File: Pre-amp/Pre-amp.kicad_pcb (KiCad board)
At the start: 2 copper layers, 80 x 53.3 mm, 52 parts, among them J1 In, J2 Send, J3 Return, J4 Out, J5 PWR, U1 LF353N, U2 LF353N, U3 LF353N

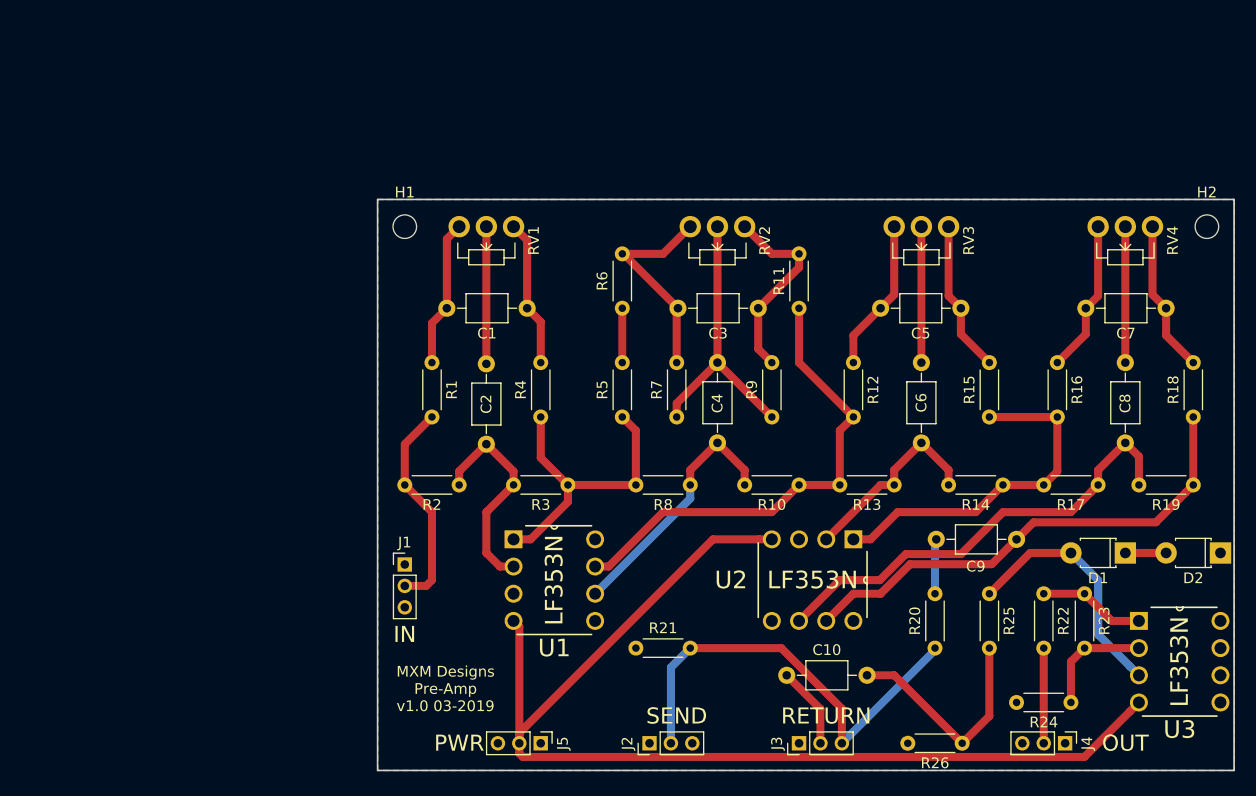
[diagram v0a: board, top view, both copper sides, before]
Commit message: Add buffer input to pre-amp
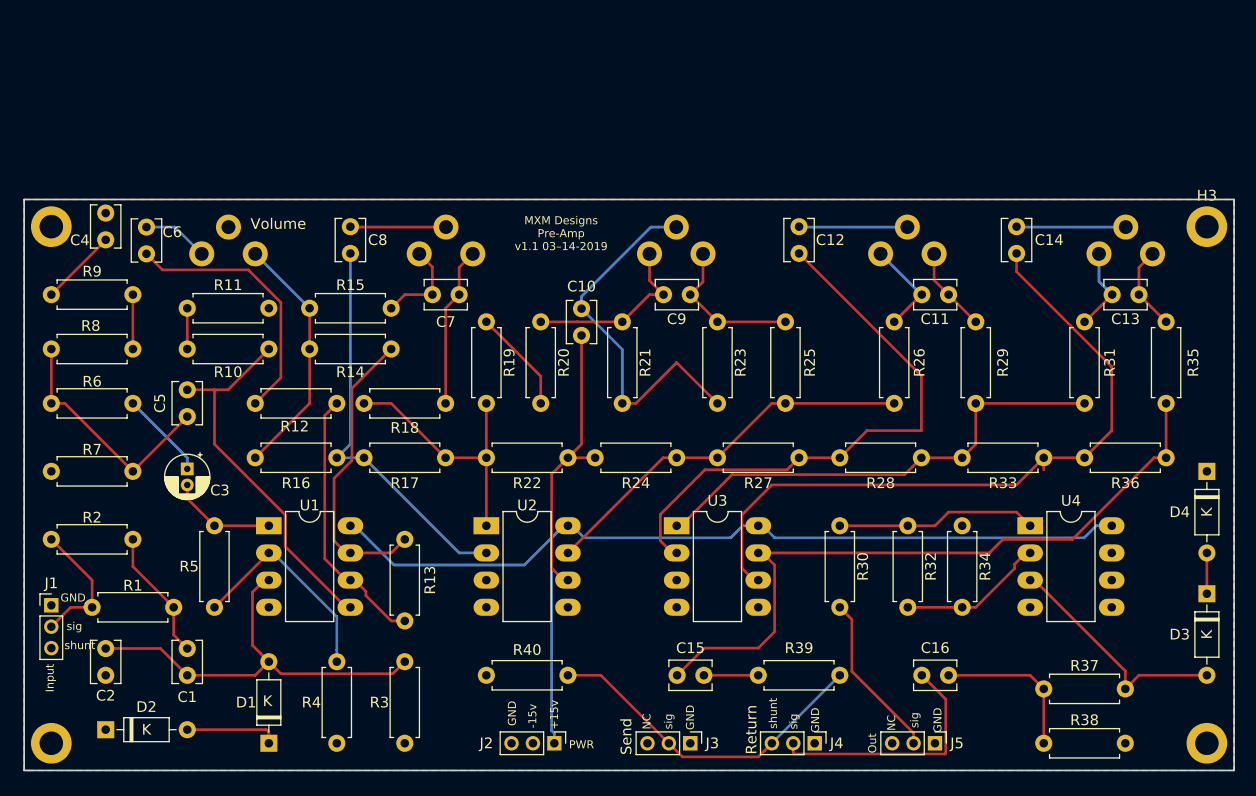
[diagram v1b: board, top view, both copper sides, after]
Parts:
- added C11: .01, Capacitor_THT:C_Disc_D3.8mm_W2.6mm_P2.50mm, F.Cu at (137.2, 57.1)
- added C12: .01, Capacitor_THT:C_Disc_D3.8mm_W2.6mm_P2.50mm, F.Cu at (123.2, 50.8)
- added C13: .047, Capacitor_THT:C_Disc_D3.8mm_W2.6mm_P2.50mm, F.Cu at (154.9, 57.1)
- added C14: .47, Capacitor_THT:C_Disc_D3.8mm_W2.6mm_P2.50mm, F.Cu at (143.5, 50.8)
- added C15: .1, Capacitor_THT:C_Disc_D3.8mm_W2.6mm_P2.50mm, F.Cu at (114.3, 92.7)
- added C16: .1, Capacitor_THT:C_Disc_D3.8mm_W2.6mm_P2.50mm, F.Cu at (134.7, 92.7)
- added D3: 1N759, Diode_THT:D_DO-35_SOD27_P7.62mm_Horizontal, F.Cu at (161.3, 85.1)
- added D4: 1N759, Diode_THT:D_DO-35_SOD27_P7.62mm_Horizontal, F.Cu at (161.3, 73.7)
- added H3: MountingHole, MountingHole:MountingHole_2.2mm_M2_DIN965_Pad, F.Cu at (161.3, 50.8)
- added H4: MountingHole, MountingHole:MountingHole_2.2mm_M2_DIN965_Pad, F.Cu at (161.3, 99.1)
- added R27: 220K, Resistor_THT:R_Axial_DIN0207_L6.3mm_D2.5mm_P7.62mm_Horizontal, F.Cu at (123.2, 72.4)
- added R28: 220K, Resistor_THT:R_Axial_DIN0207_L6.3mm_D2.5mm_P7.62mm_Horizontal, F.Cu at (134.6, 72.4)
- added R29: 5.6k, Resistor_THT:R_Axial_DIN0207_L6.3mm_D2.5mm_P7.62mm_Horizontal, F.Cu at (139.7, 67.3)
- added R30: 33k, Resistor_THT:R_Axial_DIN0207_L6.3mm_D2.5mm_P7.62mm_Horizontal, F.Cu at (127.0, 78.7)
- added R31: 3.3k, Resistor_THT:R_Axial_DIN0207_L6.3mm_D2.5mm_P7.62mm_Horizontal, F.Cu at (149.9, 59.7)
- added R32: 22k, Resistor_THT:R_Axial_DIN0207_L6.3mm_D2.5mm_P7.62mm_Horizontal, F.Cu at (133.3, 78.7)
- added R33: 220K, Resistor_THT:R_Axial_DIN0207_L6.3mm_D2.5mm_P7.62mm_Horizontal, F.Cu at (146.1, 72.4)
- added R34: 5.6k, Resistor_THT:R_Axial_DIN0207_L6.3mm_D2.5mm_P7.62mm_Horizontal, F.Cu at (138.4, 86.4)
- added R35: 3.3k, Resistor_THT:R_Axial_DIN0207_L6.3mm_D2.5mm_P7.62mm_Horizontal, F.Cu at (157.5, 67.3)
- added R36: 220K, Resistor_THT:R_Axial_DIN0207_L6.3mm_D2.5mm_P7.62mm_Horizontal, F.Cu at (157.5, 72.4)
- added R37: 12k, Resistor_THT:R_Axial_DIN0207_L6.3mm_D2.5mm_P7.62mm_Horizontal, F.Cu at (153.7, 94.0)
- added R38: 220k, Resistor_THT:R_Axial_DIN0207_L6.3mm_D2.5mm_P7.62mm_Horizontal, F.Cu at (146.1, 99.1)
- added R39: 33k, Resistor_THT:R_Axial_DIN0207_L6.3mm_D2.5mm_P7.62mm_Horizontal, F.Cu at (127.0, 92.7)
- added R40: 5.6k, Resistor_THT:R_Axial_DIN0207_L6.3mm_D2.5mm_P7.62mm_Horizontal, F.Cu at (94.0, 92.7)
- added RV5: 25k-L, Potentiometer_THT:Potentiometer_ACP_CA9-H2,5_Horizontal, B.Cu at (156.2, 53.3)
- added U4: LF353N, Package_DIP:DIP-8_W7.62mm_LongPads, F.Cu at (144.8, 78.7)
- C1: value C -> .1; footprint Capacitors_THT:C_Axial_L3.8mm_D2.6mm_P7.50mm_Horizontal -> Capacitor_THT:C_Disc_D3.8mm_W2.6mm_P2.50mm
- C10, C9: value .1 -> .0022; footprint Capacitors_THT:C_Axial_L3.8mm_D2.6mm_P7.50mm_Horizontal -> Capacitor_THT:C_Disc_D3.8mm_W2.6mm_P2.50mm
- C2: value 560pF -> 100pf; footprint Capacitors_THT:C_Axial_L3.8mm_D2.6mm_P7.50mm_Horizontal -> Capacitor_THT:C_Disc_D3.8mm_W2.6mm_P2.50mm
- C3: value .0022 -> 10µF; footprint Capacitors_THT:C_Axial_L3.8mm_D2.6mm_P7.50mm_Horizontal -> Capacitor_THT:CP_Radial_D4.0mm_P1.50mm
- C4: value .0022 -> .22; footprint Capacitors_THT:C_Axial_L3.8mm_D2.6mm_P7.50mm_Horizontal -> Capacitor_THT:C_Disc_D3.8mm_W2.6mm_P2.50mm
- C5: value .01 -> .0033; footprint Capacitors_THT:C_Axial_L3.8mm_D2.6mm_P7.50mm_Horizontal -> Capacitor_THT:C_Disc_D3.8mm_W2.6mm_P2.50mm
- C6: value .01 -> 10; footprint Capacitors_THT:C_Axial_L3.8mm_D2.6mm_P7.50mm_Horizontal -> Capacitor_THT:C_Disc_D3.8mm_W2.6mm_P2.50mm
- C7: value .047 -> 560pf; footprint Capacitors_THT:C_Axial_L3.8mm_D2.6mm_P7.50mm_Horizontal -> Capacitor_THT:C_Disc_D3.8mm_W2.6mm_P2.50mm
- C8: value .47 -> 560pF; footprint Capacitors_THT:C_Axial_L3.8mm_D2.6mm_P7.50mm_Horizontal -> Capacitor_THT:C_Disc_D3.8mm_W2.6mm_P2.50mm
- D1, D2: footprint Diodes_THT:D_T-1_P5.08mm_Horizontal -> Diode_THT:D_DO-35_SOD27_P7.62mm_Horizontal
- H1, H2: value (none) -> MountingHole; footprint Mounting_Holes:MountingHole_2.2mm_M2 -> MountingHole:MountingHole_2.2mm_M2_DIN965_Pad
- J1: footprint Pin_Headers:Pin_Header_Straight_1x03_Pitch2.00mm -> Connector_PinHeader_2.00mm:PinHeader_1x03_P2.00mm_Vertical
- J2: value Send -> PWR; footprint Pin_Headers:Pin_Header_Straight_1x03_Pitch2.00mm -> Connector_PinHeader_2.00mm:PinHeader_1x03_P2.00mm_Vertical
- J3: value Return -> Send; footprint Pin_Headers:Pin_Header_Straight_1x03_Pitch2.00mm -> Connector_PinHeader_2.00mm:PinHeader_1x03_P2.00mm_Vertical
- J4: value Out -> Return; footprint Pin_Headers:Pin_Header_Straight_1x03_Pitch2.00mm -> Connector_PinHeader_2.00mm:PinHeader_1x03_P2.00mm_Vertical
- J5: value PWR -> Out; footprint Pin_Headers:Pin_Header_Straight_1x03_Pitch2.00mm -> Connector_PinHeader_2.00mm:PinHeader_1x03_P2.00mm_Vertical
- R1: value 3.3k -> 33k; footprint Resistors_THT:R_Axial_DIN0204_L3.6mm_D1.6mm_P5.08mm_Horizontal -> Resistor_THT:R_Axial_DIN0207_L6.3mm_D2.5mm_P7.62mm_Horizontal
- R10: value 220K -> 22k; footprint Resistors_THT:R_Axial_DIN0204_L3.6mm_D1.6mm_P5.08mm_Horizontal -> Resistor_THT:R_Axial_DIN0207_L6.3mm_D2.5mm_P7.62mm_Horizontal
- R11: value 5.6k -> 22k; footprint Resistors_THT:R_Axial_DIN0204_L3.6mm_D1.6mm_P5.08mm_Horizontal -> Resistor_THT:R_Axial_DIN0207_L6.3mm_D2.5mm_P7.62mm_Horizontal
- R12: value 5.6k -> 1k; footprint Resistors_THT:R_Axial_DIN0204_L3.6mm_D1.6mm_P5.08mm_Horizontal -> Resistor_THT:R_Axial_DIN0207_L6.3mm_D2.5mm_P7.62mm_Horizontal
- R13: value 220K -> 82k; footprint Resistors_THT:R_Axial_DIN0204_L3.6mm_D1.6mm_P5.08mm_Horizontal -> Resistor_THT:R_Axial_DIN0207_L6.3mm_D2.5mm_P7.62mm_Horizontal
- R14: value 220K -> 3.3k; footprint Resistors_THT:R_Axial_DIN0204_L3.6mm_D1.6mm_P5.08mm_Horizontal -> Resistor_THT:R_Axial_DIN0207_L6.3mm_D2.5mm_P7.62mm_Horizontal
- R15: value 5.6k -> 3.3k; footprint Resistors_THT:R_Axial_DIN0204_L3.6mm_D1.6mm_P5.08mm_Horizontal -> Resistor_THT:R_Axial_DIN0207_L6.3mm_D2.5mm_P7.62mm_Horizontal
- R16: value 3.3k -> 220K; footprint Resistors_THT:R_Axial_DIN0204_L3.6mm_D1.6mm_P5.08mm_Horizontal -> Resistor_THT:R_Axial_DIN0207_L6.3mm_D2.5mm_P7.62mm_Horizontal
- R17, R18, R4: footprint Resistors_THT:R_Axial_DIN0204_L3.6mm_D1.6mm_P5.08mm_Horizontal -> Resistor_THT:R_Axial_DIN0207_L6.3mm_D2.5mm_P7.62mm_Horizontal
- R19: value 220K -> 5.6k; footprint Resistors_THT:R_Axial_DIN0204_L3.6mm_D1.6mm_P5.08mm_Horizontal -> Resistor_THT:R_Axial_DIN0207_L6.3mm_D2.5mm_P7.62mm_Horizontal
- R2: value 220K -> 23k; footprint Resistors_THT:R_Axial_DIN0204_L3.6mm_D1.6mm_P5.08mm_Horizontal -> Resistor_THT:R_Axial_DIN0207_L6.3mm_D2.5mm_P7.62mm_Horizontal
- R20: value 33k -> 12k; footprint Resistors_THT:R_Axial_DIN0204_L3.6mm_D1.6mm_P5.08mm_Horizontal -> Resistor_THT:R_Axial_DIN0207_L6.3mm_D2.5mm_P7.62mm_Horizontal
- R21: value 5.6k -> 12k; footprint Resistors_THT:R_Axial_DIN0204_L3.6mm_D1.6mm_P5.08mm_Horizontal -> Resistor_THT:R_Axial_DIN0207_L6.3mm_D2.5mm_P7.62mm_Horizontal
- R22: value 33k -> 220K; footprint Resistors_THT:R_Axial_DIN0204_L3.6mm_D1.6mm_P5.08mm_Horizontal -> Resistor_THT:R_Axial_DIN0207_L6.3mm_D2.5mm_P7.62mm_Horizontal
- R23: value 22k -> 12k; footprint Resistors_THT:R_Axial_DIN0204_L3.6mm_D1.6mm_P5.08mm_Horizontal -> Resistor_THT:R_Axial_DIN0207_L6.3mm_D2.5mm_P7.62mm_Horizontal
- R24: value 5.6k -> 220K; footprint Resistors_THT:R_Axial_DIN0204_L3.6mm_D1.6mm_P5.08mm_Horizontal -> Resistor_THT:R_Axial_DIN0207_L6.3mm_D2.5mm_P7.62mm_Horizontal
- R25: value 12k -> 5.6k; footprint Resistors_THT:R_Axial_DIN0204_L3.6mm_D1.6mm_P5.08mm_Horizontal -> Resistor_THT:R_Axial_DIN0207_L6.3mm_D2.5mm_P7.62mm_Horizontal
- R26: value 220k -> 5.6k; footprint Resistors_THT:R_Axial_DIN0204_L3.6mm_D1.6mm_P5.08mm_Horizontal -> Resistor_THT:R_Axial_DIN0207_L6.3mm_D2.5mm_P7.62mm_Horizontal
- R3: value 220K -> 220k; footprint Resistors_THT:R_Axial_DIN0204_L3.6mm_D1.6mm_P5.08mm_Horizontal -> Resistor_THT:R_Axial_DIN0207_L6.3mm_D2.5mm_P7.62mm_Horizontal
- R5: value 5.6k -> 33k; footprint Resistors_THT:R_Axial_DIN0204_L3.6mm_D1.6mm_P5.08mm_Horizontal -> Resistor_THT:R_Axial_DIN0207_L6.3mm_D2.5mm_P7.62mm_Horizontal
- R6: value 12k -> 3.3k; footprint Resistors_THT:R_Axial_DIN0204_L3.6mm_D1.6mm_P5.08mm_Horizontal -> Resistor_THT:R_Axial_DIN0207_L6.3mm_D2.5mm_P7.62mm_Horizontal
- R7: value 12k -> 22k; footprint Resistors_THT:R_Axial_DIN0204_L3.6mm_D1.6mm_P5.08mm_Horizontal -> Resistor_THT:R_Axial_DIN0207_L6.3mm_D2.5mm_P7.62mm_Horizontal
- R8: value 220K -> 12k; footprint Resistors_THT:R_Axial_DIN0204_L3.6mm_D1.6mm_P5.08mm_Horizontal -> Resistor_THT:R_Axial_DIN0207_L6.3mm_D2.5mm_P7.62mm_Horizontal
- R9: value 12k -> 1k; footprint Resistors_THT:R_Axial_DIN0204_L3.6mm_D1.6mm_P5.08mm_Horizontal -> Resistor_THT:R_Axial_DIN0207_L6.3mm_D2.5mm_P7.62mm_Horizontal
- RV1, RV4: footprint Potentiometers:Potentiometer_WirePads_Small -> Potentiometer_THT:Potentiometer_ACP_CA9-H2,5_Horizontal; moved to B.Cu
- RV2: value 25k-A -> 25k-L; footprint Potentiometers:Potentiometer_WirePads_Small -> Potentiometer_THT:Potentiometer_ACP_CA9-H2,5_Horizontal; moved to B.Cu
- RV3: value 25k-L -> 25k-A; footprint Potentiometers:Potentiometer_WirePads_Small -> Potentiometer_THT:Potentiometer_ACP_CA9-H2,5_Horizontal; moved to B.Cu
- U1, U2, U3: footprint LF351N:DIP254P762X533-8 -> Package_DIP:DIP-8_W7.62mm_LongPads
- moved H2 107.9 mm to (53.3, 50.8)
- moved D2 105.4 mm to (58.4, 97.8), turned to 0 degrees
- moved D1 82.0 mm to (73.7, 99.1), turned to 90 degrees
- moved R18 77.5 mm to (82.5, 67.3), turned to 0 degrees
- moved C8 73.5 mm to (81.3, 50.8)
- moved C6 73.1 mm to (62.2, 53.3), turned to 90 degrees
- moved C5 73.0 mm to (66.0, 68.5), turned to 90 degrees
- moved R9 68.3 mm to (53.3, 57.1), turned to 0 degrees
- moved R16 67.9 mm to (80.0, 72.4), turned to 180 degrees
- moved R19 66.5 mm to (94.0, 67.3), turned to 90 degrees
- moved C7 66.1 mm to (91.4, 57.1)
- moved R14 66.0 mm to (77.5, 62.2), turned to 0 degrees
- moved R17 61.0 mm to (90.2, 72.4)
- moved R7 58.6 mm to (53.3, 73.7), turned to 0 degrees
- moved R10 58.5 mm to (66.0, 62.2), turned to 0 degrees
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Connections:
- C2 pad 1: Net-(C2-Pad1) -> GND
- C2 pad 2: Net-(C2-Pad2) -> Net-(C1-Pad1)
- C4 pad 2: Net-(C4-Pad2) -> GND
- D1 pad 2: Net-(D1-Pad2) -> Net-(C1-Pad1)
- J2 pad 1: GND -> +15V
- J2 pad 2: Net-(J2-Pad2) -> -15V
- J2 pad 3: (no net) -> GND
- J3 pad 2: Net-(C10-Pad1) -> Net-(J3-Pad2)
- J3 pad 3: Net-(J2-Pad2) -> Net-(J3-Pad3)
- J4 pad 2: Net-(J4-Pad2) -> Net-(C16-Pad1)
- J4 pad 3: (no net) -> Net-(J3-Pad2)
- J5 pad 1: +15V -> GND
- J5 pad 2: -15V -> Net-(J5-Pad2)
- J5 pad 3: GND -> Net-(J5-Pad3)
- R10 pad 2: Net-(C4-Pad2) -> Net-(C5-Pad2)
- R11 pad 1: Net-(R10-Pad1) -> GND
- R11 pad 2: Net-(C3-Pad1) -> Net-(R10-Pad1)
- R12 pad 1: Net-(C5-Pad2) -> Net-(C6-Pad1)
- R12 pad 2: Net-(R10-Pad1) -> Net-(R12-Pad2)
- R13 pad 1: Net-(C6-Pad2) -> Net-(R13-Pad1)
- R13 pad 2: Net-(R10-Pad1) -> Net-(R12-Pad2)
- R14 pad 2: Net-(C6-Pad2) -> Net-(R13-Pad1)
- R15 pad 1: Net-(R14-Pad1) -> Net-(C7-Pad2)
- R15 pad 2: Net-(C5-Pad1) -> Net-(R14-Pad1)
- R16 pad 1: Net-(C7-Pad2) -> Net-(C8-Pad2)
- R17 pad 1: Net-(C8-Pad2) -> Net-(R17-Pad1)
- R17 pad 2: Net-(R14-Pad1) -> Net-(C8-Pad2)
- R18 pad 1: Net-(C9-Pad2) -> Net-(R17-Pad1)
- R19 pad 1: Net-(C9-Pad2) -> Net-(R17-Pad1)
- R19 pad 2: Net-(C8-Pad2) -> Net-(R19-Pad2)
- R2 pad 1: Net-(C2-Pad2) -> Net-(C1-Pad2)
- R20 pad 1: Net-(J2-Pad2) -> Net-(R19-Pad2)
- R20 pad 2: Net-(C9-Pad1) -> Net-(C9-Pad2)
- R21 pad 1: GND -> Net-(C10-Pad1)
- R21 pad 2: Net-(J2-Pad2) -> Net-(C9-Pad2)
- R22 pad 1: Net-(R22-Pad1) -> Net-(C10-Pad2)
- R22 pad 2: Net-(J4-Pad2) -> Net-(R17-Pad1)
- R23 pad 1: Net-(R22-Pad1) -> Net-(C10-Pad1)
- R23 pad 2: Net-(R23-Pad2) -> Net-(C9-Pad1)
- R24 pad 1: Net-(R23-Pad2) -> Net-(R24-Pad1)
- R24 pad 2: GND -> Net-(C10-Pad2)
- R25 pad 1: Net-(D1-Pad2) -> Net-(R24-Pad1)
- R25 pad 2: Net-(C10-Pad2) -> Net-(C9-Pad1)
- R26 pad 1: Net-(C10-Pad2) -> Net-(C11-Pad2)
- R26 pad 2: GND -> Net-(R24-Pad1)
- R3 pad 1: Net-(R3-Pad1) -> GND
- R3 pad 2: Net-(C2-Pad2) -> Net-(C1-Pad1)
- R4 pad 1: Net-(R3-Pad1) -> GND
- R4 pad 2: Net-(C1-Pad1) -> Net-(R4-Pad2)
- R5 pad 1: Net-(R3-Pad1) -> Net-(R4-Pad2)
- R5 pad 2: Net-(R5-Pad2) -> Net-(C3-Pad2)
- R6 pad 1: Net-(R5-Pad2) -> Net-(C5-Pad1)
- R6 pad 2: Net-(C3-Pad2) -> Net-(C3-Pad1)
- R7 pad 1: Net-(C4-Pad1) -> GND
- R7 pad 2: Net-(C3-Pad2) -> Net-(C5-Pad1)
- R8 pad 1: Net-(C4-Pad2) -> Net-(R8-Pad1)
- R8 pad 2: Net-(R3-Pad1) -> Net-(C5-Pad1)
- R9 pad 2: Net-(C3-Pad1) -> Net-(R8-Pad1)
- RV1 pad 1: Net-(C1-Pad1) -> Net-(R14-Pad1)
- RV1 pad 2: Net-(C2-Pad1) -> GND
- RV1 pad 3: Net-(C1-Pad2) -> Net-(C6-Pad2)
- RV2 pad 1: Net-(C3-Pad1) -> Net-(C7-Pad1)
- RV2 pad 2: Net-(C4-Pad1) -> Net-(C8-Pad1)
- RV2 pad 3: Net-(C3-Pad2) -> Net-(C7-Pad2)
- RV3 pad 1: Net-(C5-Pad1) -> Net-(C9-Pad1)
- RV3 pad 2: Net-(C6-Pad1) -> Net-(C10-Pad1)
- RV3 pad 3: Net-(C5-Pad2) -> Net-(C9-Pad2)
- RV4 pad 1: Net-(C7-Pad1) -> Net-(C11-Pad1)
- RV4 pad 2: Net-(C8-Pad1) -> Net-(C12-Pad1)
- RV4 pad 3: Net-(C7-Pad2) -> Net-(C11-Pad2)
- U1 pad 1: Net-(R3-Pad1) -> Net-(C3-Pad2)
- U1 pad 2: Net-(C2-Pad2) -> Net-(R4-Pad2)
- U1 pad 3: GND -> Net-(C1-Pad1)
- U1 pad 5: GND -> Net-(C5-Pad2)
- U1 pad 6: Net-(C4-Pad2) -> Net-(R12-Pad2)
- U1 pad 7: Net-(R10-Pad1) -> Net-(R13-Pad1)
- U2 pad 1: Net-(R14-Pad1) -> Net-(R17-Pad1)
- U2 pad 2: Net-(C6-Pad2) -> Net-(C8-Pad2)
- U2 pad 6: Net-(C8-Pad2) -> Net-(C10-Pad2)
- U2 pad 7: Net-(C9-Pad2) -> Net-(R24-Pad1)
- U3 pad 1: Net-(R22-Pad1) -> Net-(R28-Pad1)
- U3 pad 2: Net-(R23-Pad2) -> Net-(C12-Pad2)
- U3 pad 3: Net-(D1-Pad2) -> GND
- U3 pad 5: (no net) -> GND
- U3 pad 6: (no net) -> Net-(C14-Pad2)
- U3 pad 7: (no net) -> Net-(C15-Pad2)
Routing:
- net -15V: track 104.8 -> 0.00 mm
- net +15V: track 0.00 -> 96.9 mm
- net Net-(C15-Pad2): track 0.00 -> 66.3 mm
- net Net-(C14-Pad2): track 0.00 -> 66.1 mm
- net Net-(C12-Pad2): track 0.00 -> 53.4 mm
- net Net-(R28-Pad1): track 0.00 -> 45.1 mm
- net Net-(J2-Pad2): track 41.9 -> 0.00 mm
- net Net-(R10-Pad1): track 45.2 -> 3.81 mm
- net Net-(R24-Pad1): track 0.00 -> 36.3 mm
- net Net-(J3-Pad2): track 0.00 -> 31.7 mm
- net Net-(C9-Pad2): track 45.9 -> 16.9 mm
- net Net-(R3-Pad1): track 28.7 -> 0.00 mm
- net Net-(R13-Pad1): track 0.00 -> 27.7 mm
- net Net-(C10-Pad1): track 7.65 -> 35.1 mm
- net Net-(C1-Pad1): track 13.8 -> 39.6 mm
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- added copper zone on B.Cu, net -15V
- removed copper zone on B.Cu, net +15V
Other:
- board size 80 x 53.3 mm -> 113 x 53.3 mm
- board text added: "+15v"
- board text added: "-15v"
- board text added: "GND"
- board text added: "Input"
- board text added: "MXM Designs Pre-Amp v1.1 03–14-2019"
- board text added: "NC"
- board text added: "Out"
- board text added: "Volume"
- board text added: "shunt"
- board text added: "sig"
- board text removed: "IN"
- board text removed: "MXM Designs Pre-Amp v1.0 03-2019"
- board text removed: "OUT"
- board text removed: "RETURN"
- board text removed: "SEND"

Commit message: update version
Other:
- board text added: "MXM Designs Pre-Amp v1.1.1 04–01-2019"
- board text removed: "MXM Designs Pre-Amp v1.1 03–14-2019"
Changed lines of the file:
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@@
-(kicad_pcb (version 20171130) (host pcbnew "(5.0.2-5-10.14)")
+(kicad_pcb (version 20171130) (host pcbnew "(5.1.0-0)")
   (general
     (thickness 1.6)
@@
     (46 B.CrtYd user)
     (47 F.CrtYd user hide)
-    (48 B.Fab user hide)
-    (49 F.Fab user hide)
+    (48 B.Fab user)
+    (49 F.Fab user)
   )
   (setup
@@
     (zone_45_only no)
     (trace_min 0.2)
-    (segment_width 0.2)
-    (edge_width 0.15)
     (via_size 0.8)
     (via_drill 0.4)
@@
     (uvia_min_size 0.2)
     (uvia_min_drill 0.1)
+    (edge_width 0.15)
+    (segment_width 0.2)
     (pcb_text_width 0.3)
     (pcb_text_size 1.5 1.5)
@@
       (effects (font (size 1 1) (thickness 0.15)))
     )
-    (fp_text value 22k (at 3.81 2.37 180) (layer F.Fab)
+    (fp_text value 22k (at 3.81 0 180) (layer F.SilkS)
       (effects (font (size 1 1) (thickness 0.15)))
     )
@@
       (effects (font (size 1 1) (thickness 0.15)))
     )
-    (fp_text value 3.3k (at 3.81 2.37 180) (layer F.Fab)
+    (fp_text value 3.3k (at 3.556 0 180) (layer F.SilkS)
       (effects (font (size 1 1) (thickness 0.15)))
     )
@@
     (effects (font (size 0.75 0.75) (thickness 0.1)))
   )
-  (gr_text "MXM Designs \nPre-Amp\nv1.1 03–14-2019" (at 100.965 51.435) (layer F.SilkS)
+  (gr_text "MXM Designs \nPre-Amp\nv1.1.1 04–01-2019" (at 100.965 51.435) (layer F.SilkS)
     (effects (font (size 0.75 0.75) (thickness 0.1)))
   )

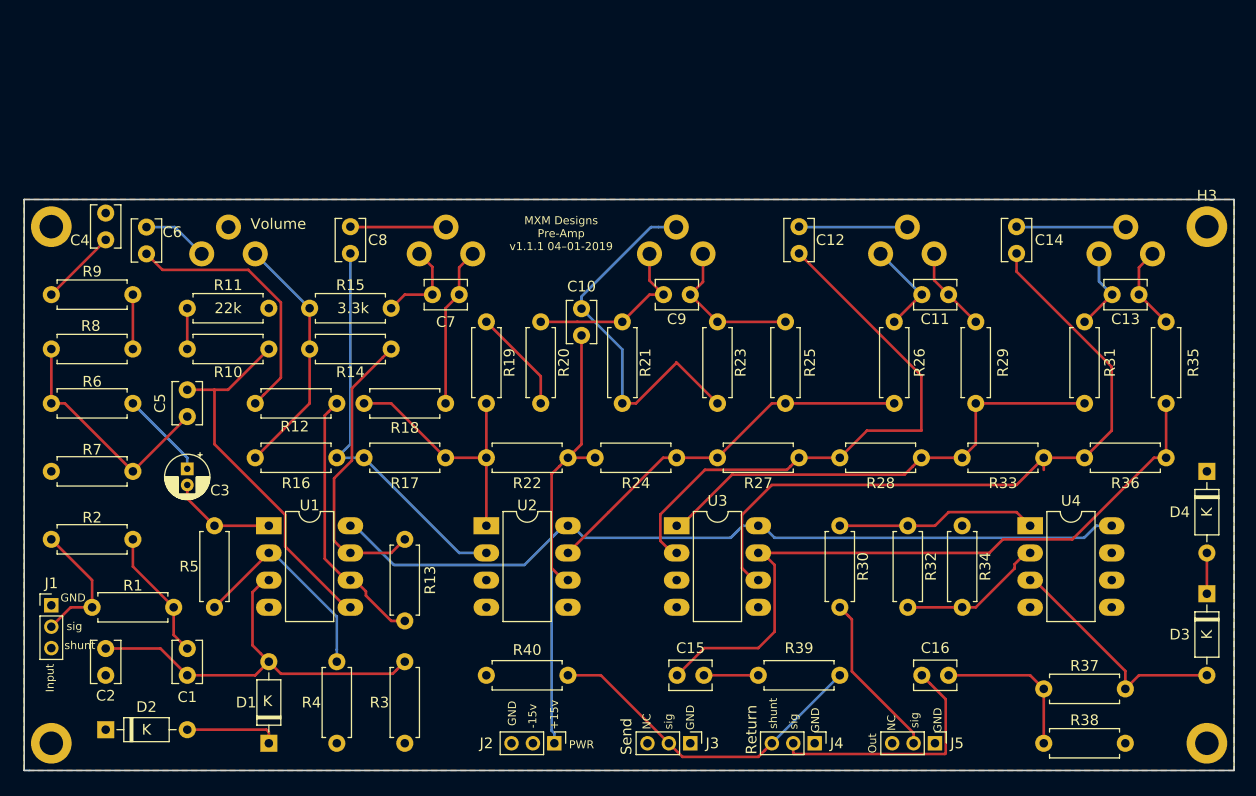
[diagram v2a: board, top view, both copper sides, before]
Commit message: update layout move vaules to silkscreen layer. Change some routes to give more room around pads.
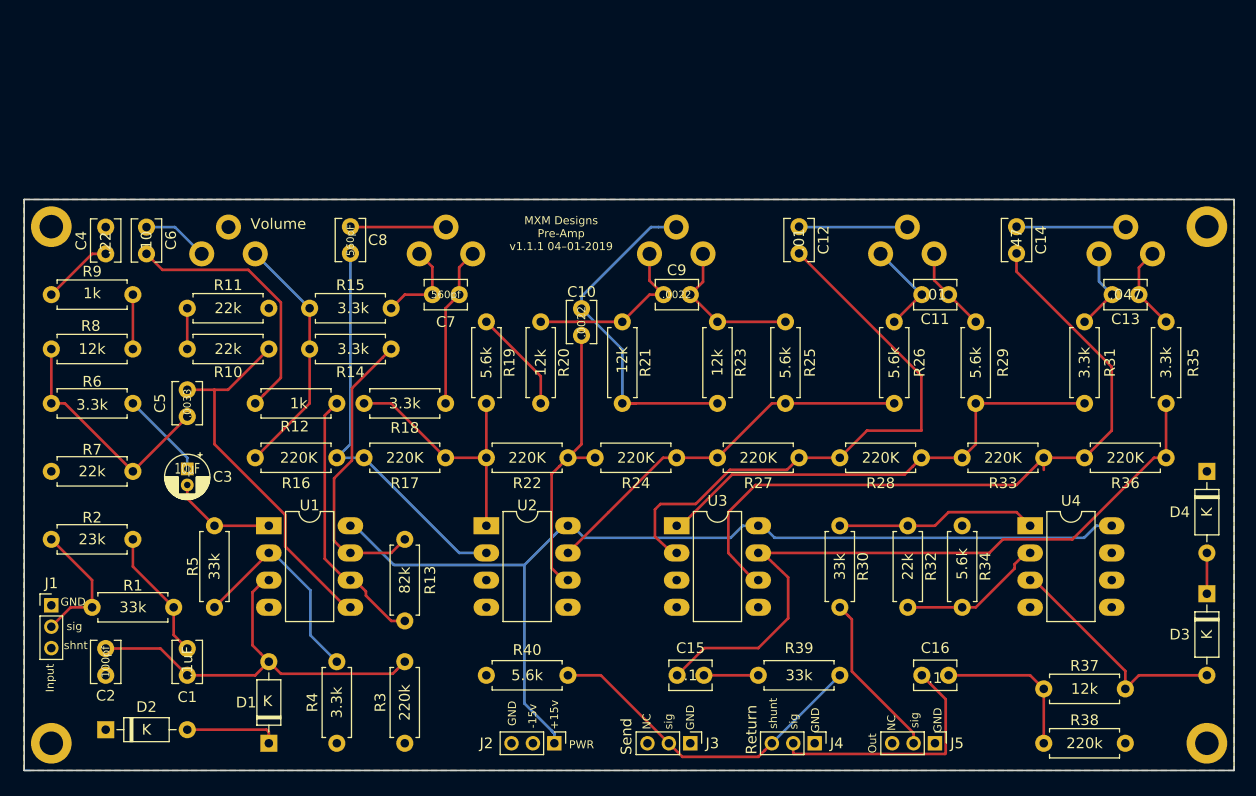
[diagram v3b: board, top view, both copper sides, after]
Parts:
- C1: value .1 -> .1uF
- moved C4 1.31 mm to (58.4, 53.3)
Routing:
- net Net-(C14-Pad2): track 66.1 -> 68.0 mm
- net Net-(C10-Pad1): track 35.1 -> 33.3 mm
- net +15V: track 96.9 -> 95.8 mm
- net Net-(C15-Pad2): track 66.3 -> 67.4 mm
- net Net-(C12-Pad2): track 53.4 -> 54.4 mm
- net Net-(C4-Pad1): track 7.22 -> 6.66 mm
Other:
- board text added: "shnt"

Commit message: update to pc mount pots
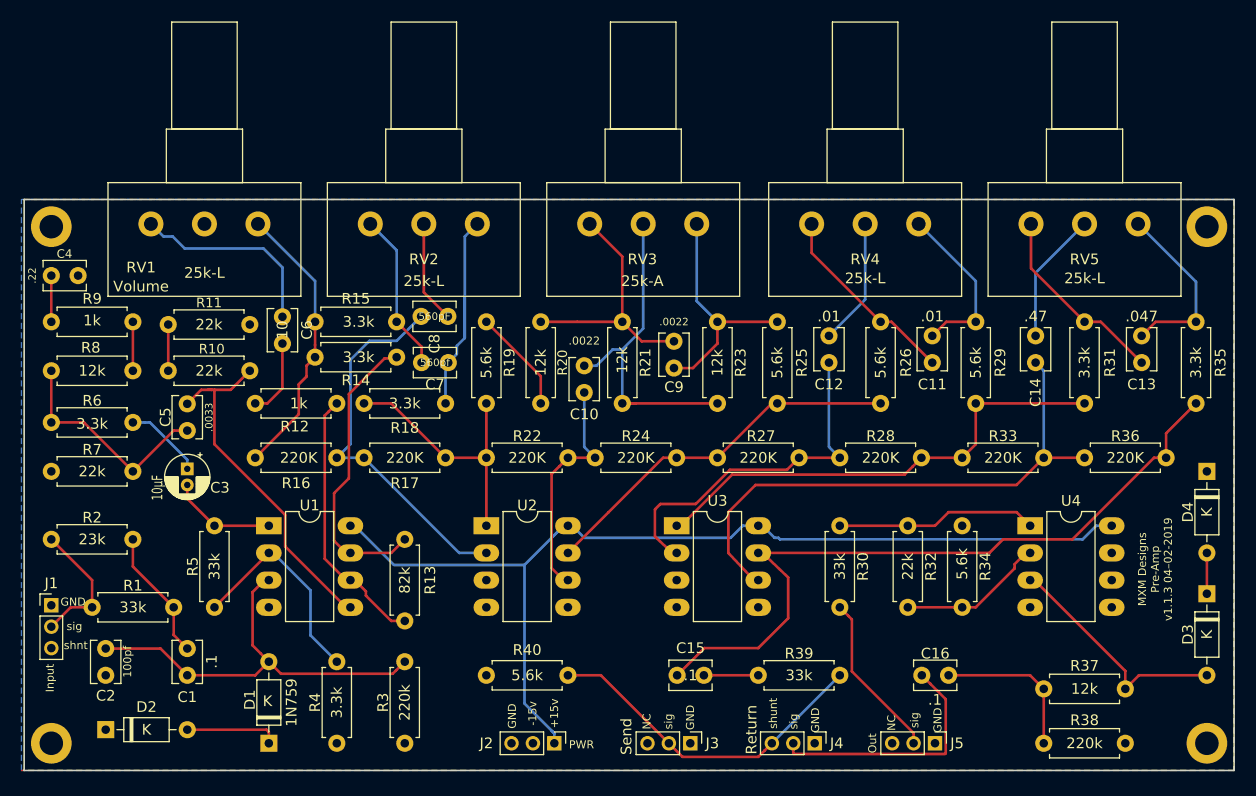
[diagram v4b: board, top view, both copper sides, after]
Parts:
- C1: value .1uF -> .1
- RV1, RV2, RV3, RV4, RV5: footprint Potentiometer_THT:Potentiometer_ACP_CA9-H2,5_Horizontal -> Potentiometers:Potentiometer_Alps_RK163_Single_Vertical; moved to F.Cu
- moved C6 15.2 mm to (74.9, 61.7)
- moved C8 12.4 mm to (90.4, 59.2), turned to 180 degrees
- moved C12 10.6 mm to (126.0, 61.0)
- moved C14 10.4 mm to (145.3, 61.0)
- moved C9 7.03 mm to (111.5, 64.0), turned to 90 degrees
- moved C7 6.43 mm to (90.4, 63.5)
- moved C4 5.47 mm to (53.3, 55.4), turned to 0 degrees
- moved C10 5.34 mm to (103.1, 63.8)
- moved C11 4.14 mm to (135.6, 61.0), turned to 270 degrees
- moved C13 3.86 mm to (155.2, 61.0), turned to 270 degrees
- moved RV4 3.15 mm to (134.4, 50.5)
- moved RV5 3.10 mm to (154.9, 50.5)
- moved RV3 2.86 mm to (113.6, 50.5)
- moved RV2 2.83 mm to (93.1, 50.5)
- moved RV1 2.81 mm to (72.6, 50.5)
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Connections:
- J3 pad 3: Net-(J3-Pad3) -> (no net)
- J5 pad 3: Net-(J5-Pad3) -> (no net)
- U4 pad 5: Net-(U4-Pad5) -> (no net)
- U4 pad 6: Net-(U4-Pad6) -> (no net)
- U4 pad 7: Net-(U4-Pad7) -> (no net)
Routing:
- net Net-(C12-Pad2): track 54.4 -> 33.8 mm
- net Net-(C6-Pad1): track 24.9 -> 7.30 mm
- net Net-(C14-Pad2): track 68.0 -> 52.3 mm
- net Net-(C6-Pad2): track 6.20 -> 18.6 mm
- net Net-(C13-Pad2): track 7.95 -> 18.2 mm
- net Net-(C11-Pad2): track 9.06 -> 18.2 mm
- net Net-(C13-Pad1): track 7.93 -> 17.0 mm
- net Net-(C9-Pad1): track 14.2 -> 22.6 mm
- net Net-(C11-Pad1): track 7.96 -> 16.0 mm
- net Net-(C7-Pad1): track 15.0 -> 21.9 mm
- net Net-(C9-Pad2): track 16.9 -> 23.6 mm
- net Net-(C7-Pad2): track 8.70 -> 14.9 mm
- net Net-(C10-Pad2): track 27.4 -> 22.0 mm
- net Net-(R14-Pad1): track 23.3 -> 26.4 mm
- net Net-(C4-Pad1): track 6.66 -> 4.32 mm
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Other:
- board text added: "MXM Designs Pre-Amp v1.1.3 04–02-2019"
- board text removed: "MXM Designs Pre-Amp v1.1.1 04–01-2019"

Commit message: create new branch  1.1.4
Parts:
- C1: value .1 -> .1uf
- C14: value .47 -> .047
- C6: value 10 -> 10uF; footprint Capacitor_THT:C_Disc_D3.8mm_W2.6mm_P2.50mm -> Capacitor_THT:CP_Radial_D4.0mm_P1.50mm
- R2: value 23k -> 22k
- moved D4 20.3 mm to (161.0, 94.0), turned to 90 degrees
- moved D3 10.00 mm to (156.7, 94.0), turned to 90 degrees
- moved D2 7.62 mm to (66.0, 97.8), turned to 180 degrees
- moved C16 5.48 mm to (140.0, 94.0)
- moved C4 3.21 mm to (56.4, 56.4), turned to 90 degrees
- moved R36 2.79 mm to (160.3, 72.4)
- moved C10 2.58 mm to (103.1, 61.2)
- moved C5 1.70 mm to (64.5, 69.1), turned to 0 degrees
- moved R7 1.52 mm to (53.3, 75.2)
- moved C2 1.27 mm to (59.7, 92.7)
- moved R33 1.27 mm to (147.3, 72.4)
- moved R14 1.15 mm to (78.1, 64.1)
- moved C8 1.06 mm to (91.4, 59.2)
- moved R6 1.02 mm to (53.3, 70.1)
- moved R8 1.02 mm to (61.0, 65.3)
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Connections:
- D2 pad 1: GND -> Net-(D1-Pad1)
- D2 pad 2: Net-(D1-Pad1) -> GND
- D4 pad 2: Net-(D3-Pad1) -> Net-(D3-Pad2)
- J3 pad 3: (no net) -> Net-(J3-Pad3)
- J5 pad 3: (no net) -> Net-(J5-Pad3)
- R37 pad 1: Net-(D3-Pad2) -> Net-(D3-Pad1)
- R8 pad 1: Net-(R8-Pad1) -> Net-(R10-Pad1)
- R9 pad 2: Net-(R8-Pad1) -> Net-(R10-Pad1)
- U4 pad 3: Net-(D3-Pad2) -> Net-(D3-Pad1)
- U4 pad 5: (no net) -> GND
- U4 pad 6: (no net) -> Net-(U4-Pad6)
- U4 pad 7: (no net) -> Net-(U4-Pad6)
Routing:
- net Net-(D3-Pad2): track 22.2 -> 4.32 mm
- net Net-(D3-Pad1): track 3.81 -> 17.1 mm
- net Net-(C10-Pad2): track 22.0 -> 30.5 mm
- net Net-(R10-Pad1): track 4.32 -> 12.6 mm
- net Net-(C16-Pad2): track 14.5 -> 8.64 mm
- net Net-(R8-Pad1): track 4.57 -> 0.00 mm
- net Net-(R12-Pad2): track 25.1 -> 29.4 mm
- net Net-(C16-Pad1): track 23.4 -> 19.4 mm
- net Net-(C7-Pad1): track 21.9 -> 18.3 mm
- net Net-(C14-Pad2): track 52.3 -> 55.9 mm
- net Net-(C5-Pad2): track 33.3 -> 36.6 mm
- net Net-(C9-Pad2): track 23.6 -> 26.9 mm
- net Net-(C8-Pad2): track 35.6 -> 38.4 mm
- net Net-(U4-Pad6): track 0.00 -> 2.54 mm
- net Net-(R4-Pad2): track 20.2 -> 22.7 mm
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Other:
- board text added: "MXM Designs Pre-Amp v1.1.4 04–27-2019"
- board text removed: "MXM Designs Pre-Amp v1.1.3 04–02-2019"
